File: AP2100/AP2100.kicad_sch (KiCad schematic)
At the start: 0 parts

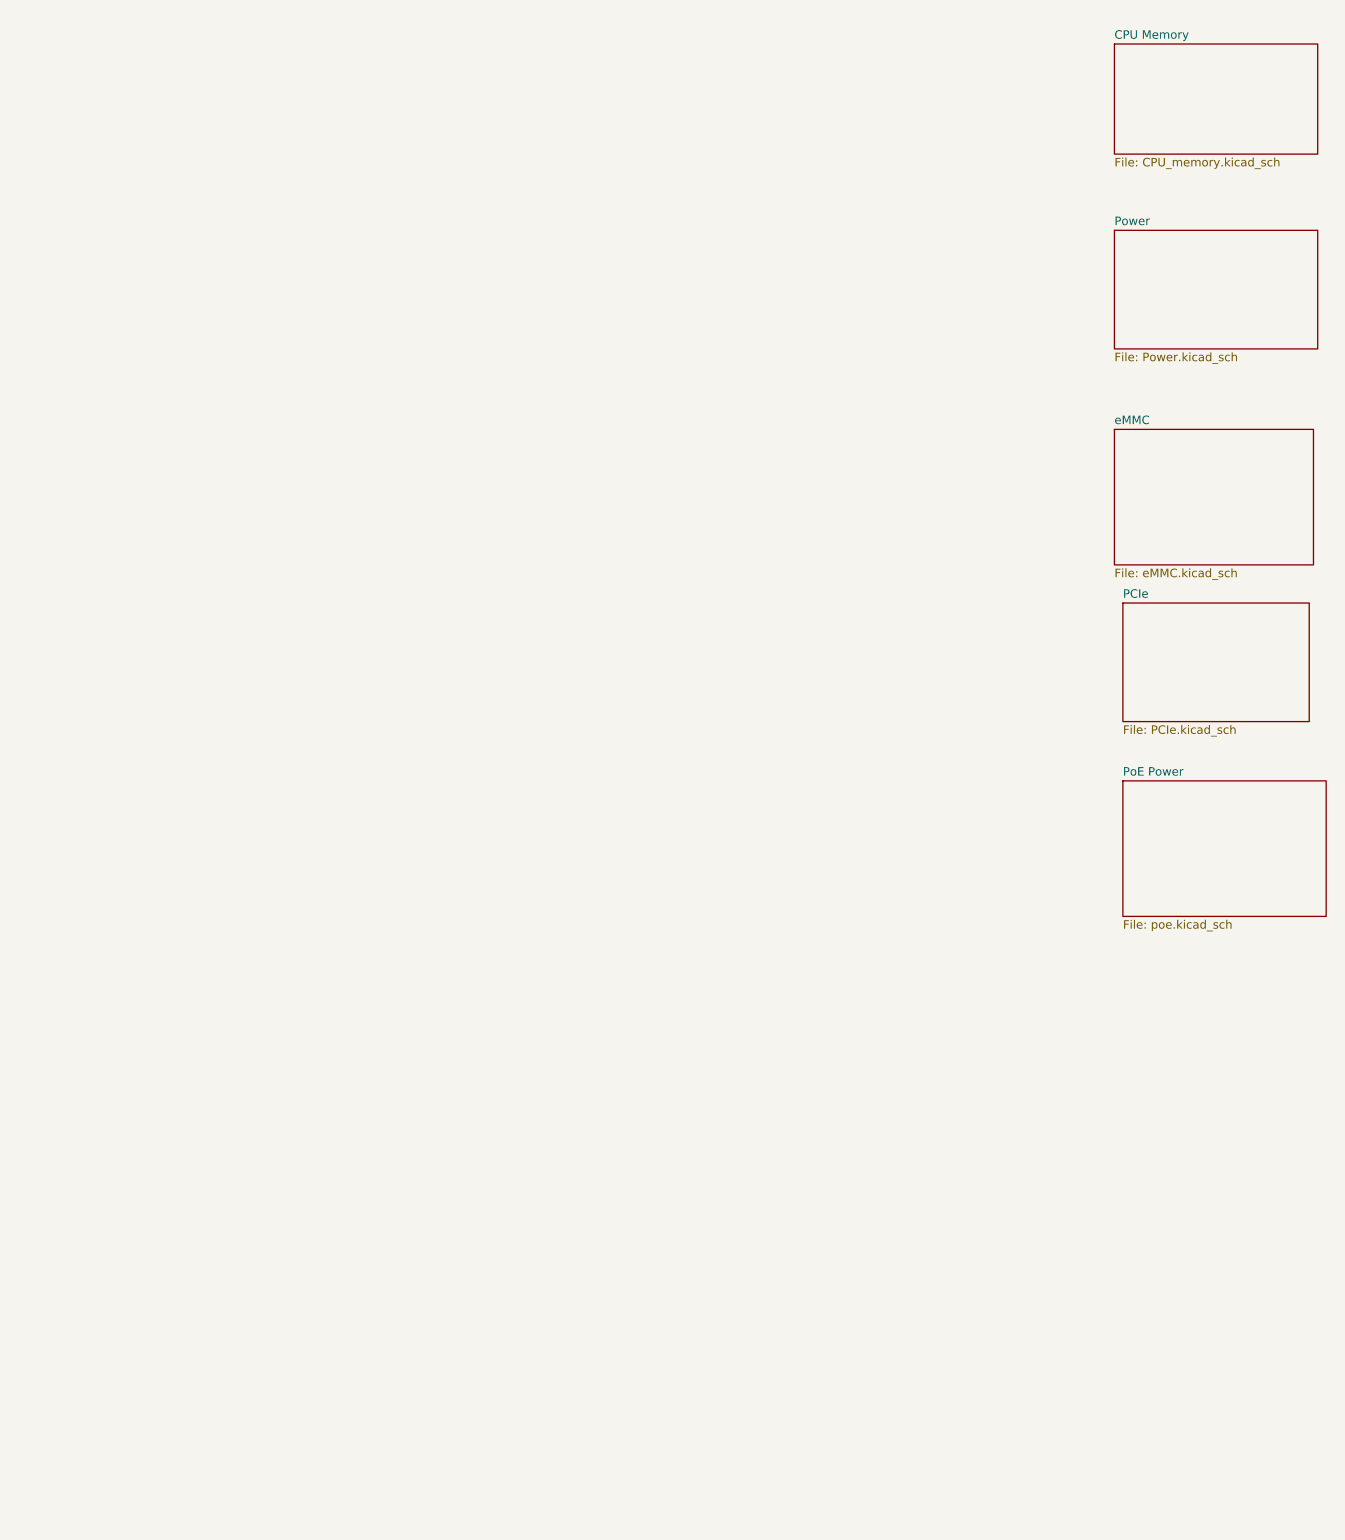
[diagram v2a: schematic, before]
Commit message: Add CPU Power block. Change global labels to hierarchical and link them at top page Add 5V USB power supply
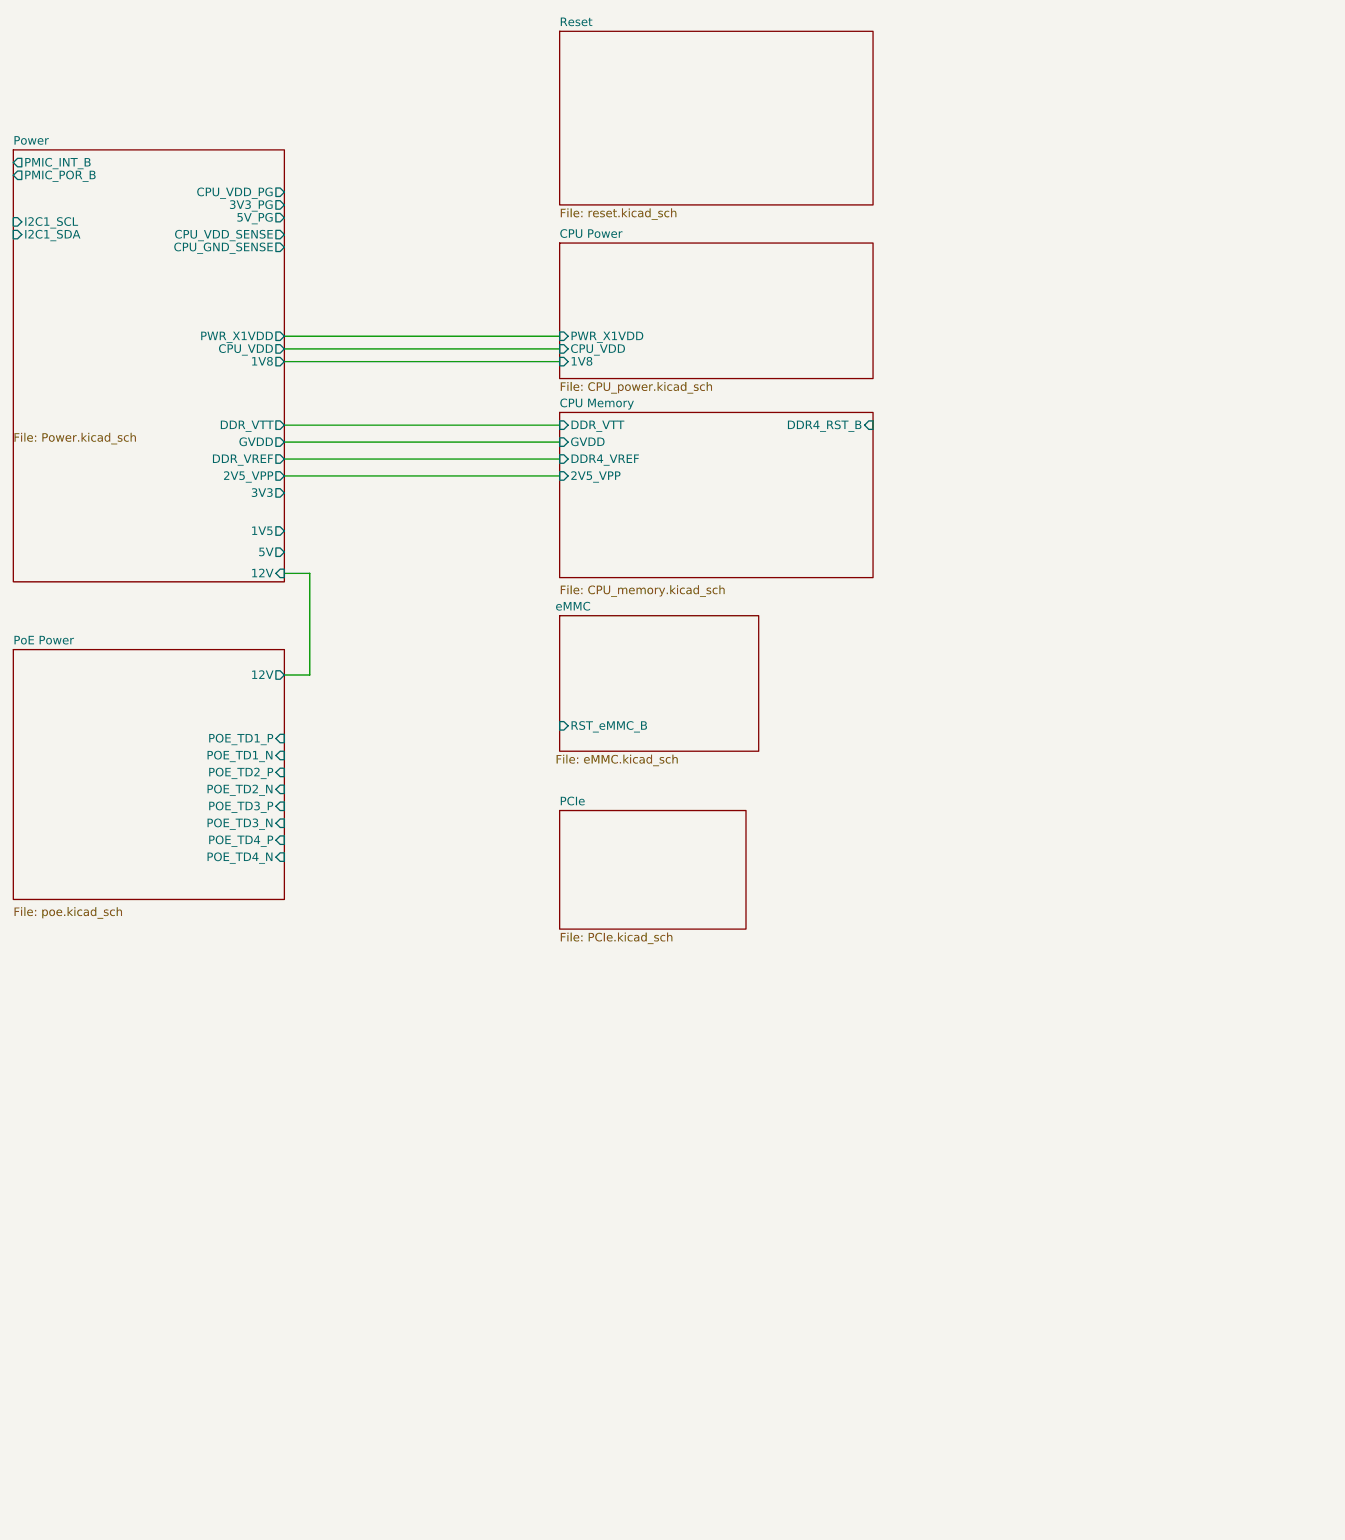
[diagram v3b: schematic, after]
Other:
- added sheet CPU Power (CPU_power.kicad_sch)
- added sheet Reset (reset.kicad_sch)
- sheet CPU Memory ports: added 2V5_VPP, DDR4_RST_B, DDR4_VREF, DDR_VTT, GVDD; removed none
- sheet PoE Power ports: added 12V, POE_TD1_N, POE_TD1_P, POE_TD2_N, POE_TD2_P, POE_TD3_N, POE_TD3_P, POE_TD4_N, POE_TD4_P; removed none
- sheet Power ports: added 12V, 1V5, 1V8, 2V5_VPP, 3V3, 3V3_PG, 5V, 5V_PG, CPU_GND_SENSE, CPU_VDD, CPU_VDD_PG, CPU_VDD_SENSE, DDR_VREF, DDR_VTT, GVDD, I2C1_SCL, I2C1_SDA, PMIC_INT_B, PMIC_POR_B, PWR_X1VDD; removed none
- sheet eMMC ports: added RST_eMMC_B; removed none

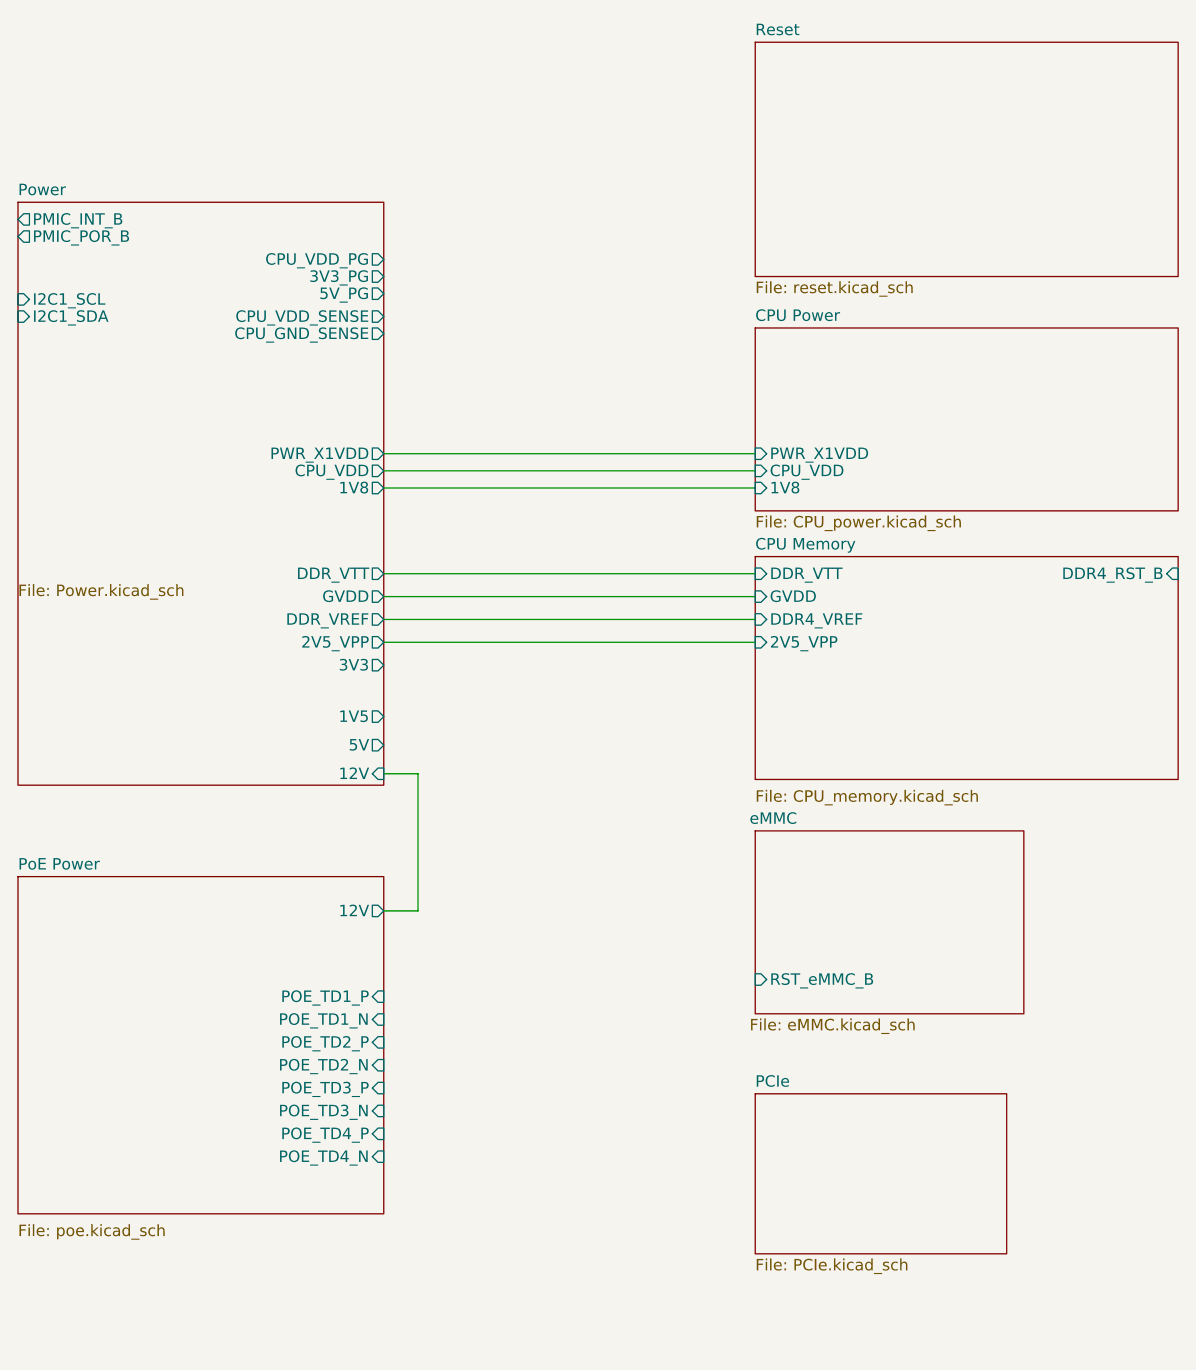
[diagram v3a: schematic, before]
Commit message: Add 2nd CPU power page. Start reset block
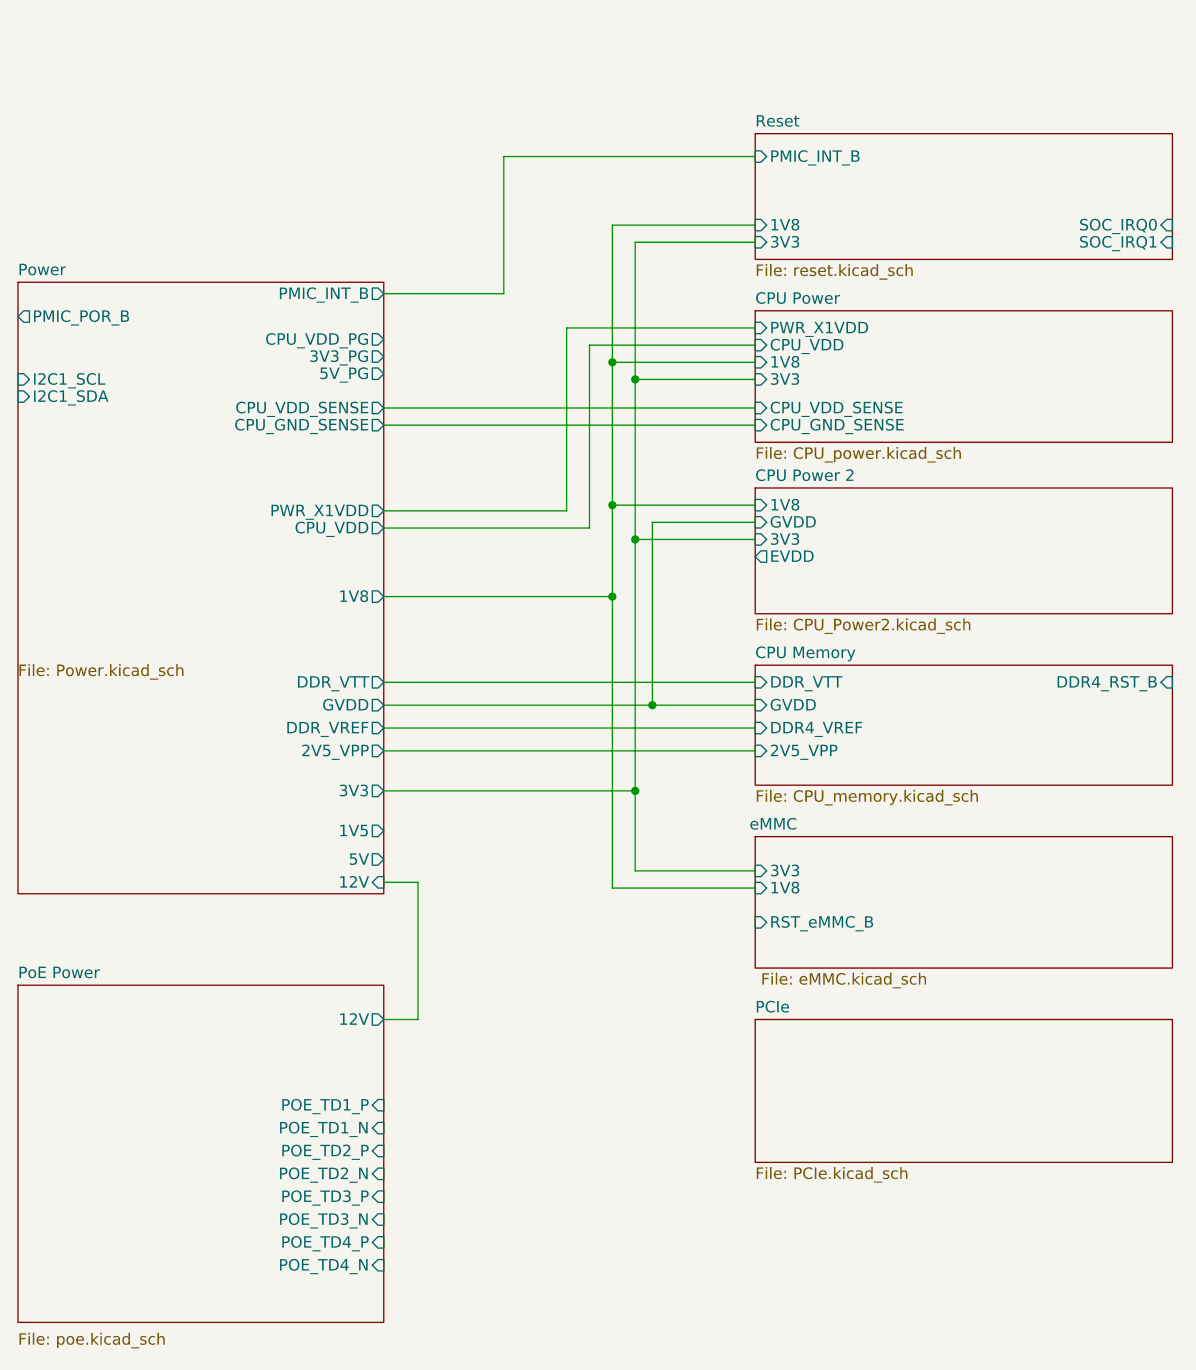
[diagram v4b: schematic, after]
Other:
- added sheet CPU Power 2 (CPU_Power2.kicad_sch)
- sheet CPU Power ports: added 3V3, CPU_GND_SENSE, CPU_VDD_SENSE; removed none
- sheet Reset ports: added 1V8, 3V3, PMIC_INT_B, SOC_IRQ0, SOC_IRQ1; removed none
- sheet eMMC ports: added 1V8, 3V3; removed none
